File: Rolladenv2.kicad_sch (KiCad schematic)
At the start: 1 part, among them U1 ESP32-S3

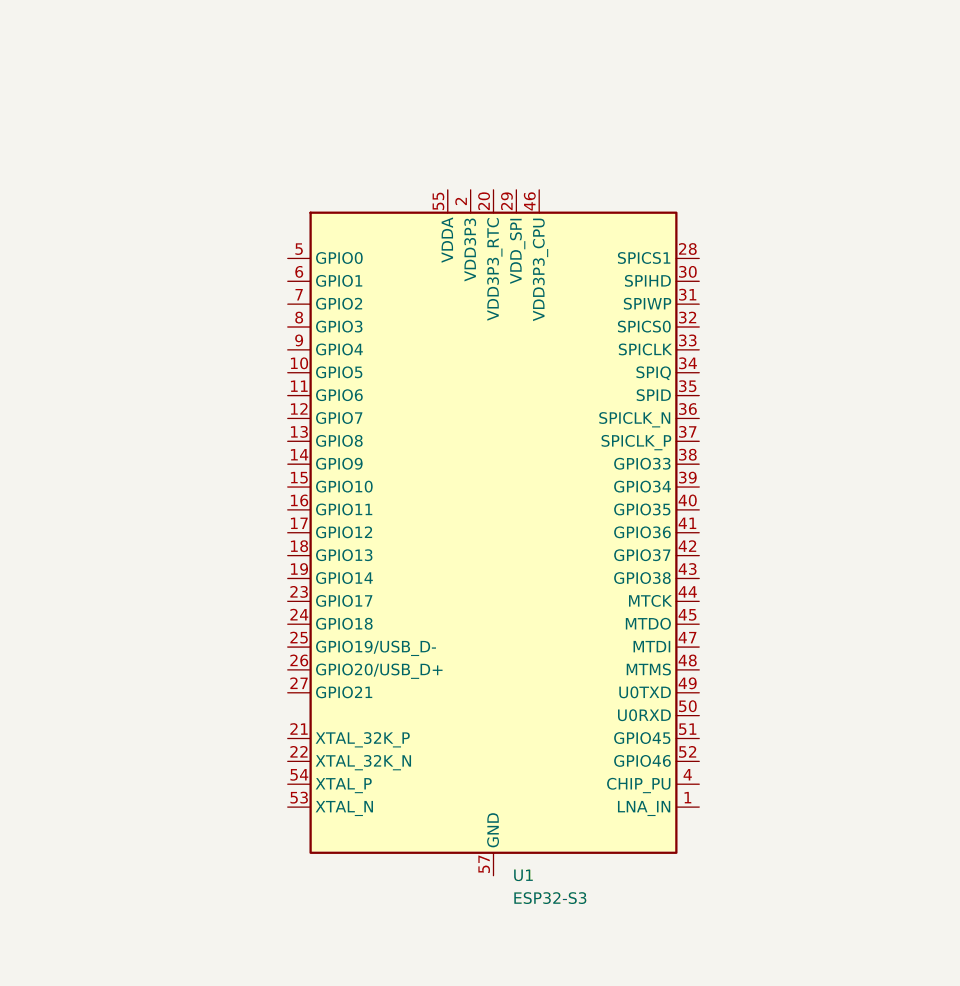
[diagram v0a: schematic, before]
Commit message: Added Caps and XTAL
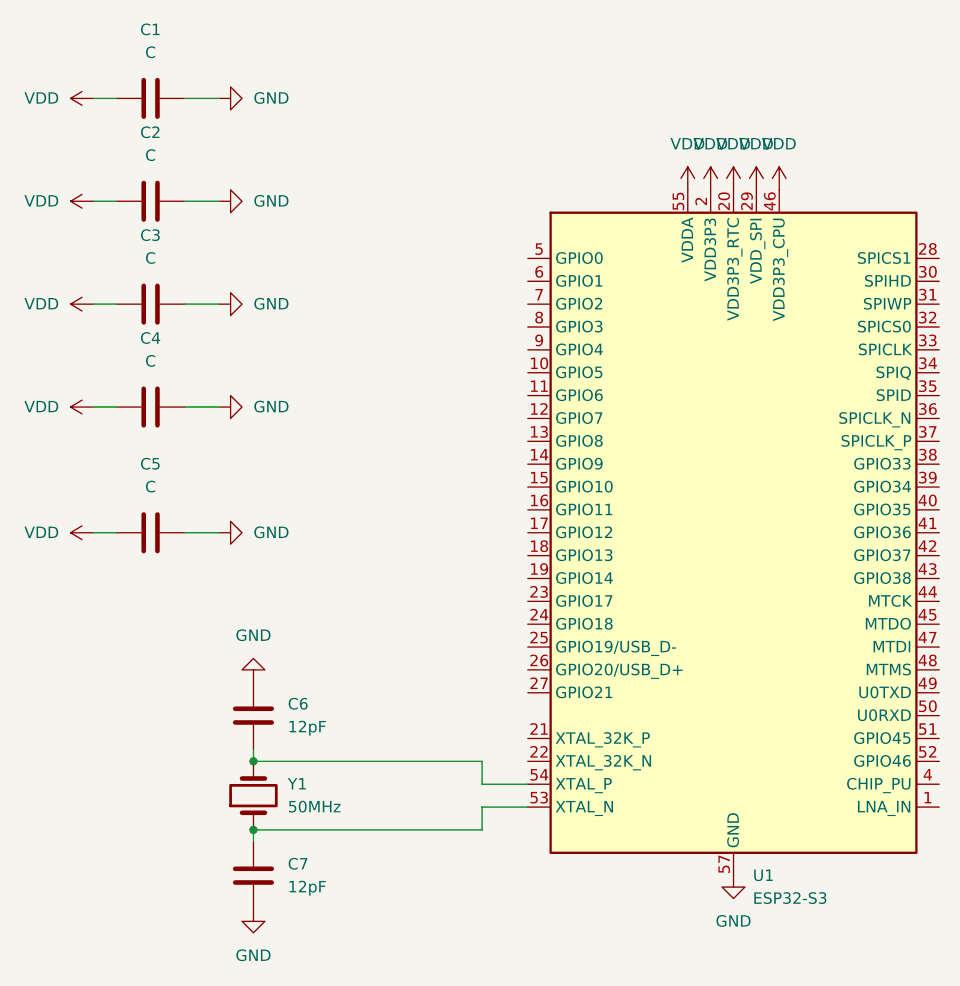
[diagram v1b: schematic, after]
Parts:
- added C1, C2, C3, C4, C5: C, Capacitor_SMD:C_0805_2012Metric_Pad1.18x1.45mm_HandSolder, symbol Device:C
- added C6, C7: 12pF, Capacitor_SMD:C_0603_1608Metric_Pad1.08x0.95mm_HandSolder, symbol Device:C
- added Y1: 50MHz, Crystal:Crystal_SMD_MicroCrystal_CC4V-T1A-2Pin_5.0x1.9mm_HandSoldering, symbol Device:Crystal
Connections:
- net VDD: now reaches U1.2 (VDD3P3), U1.3 (VDD3P3)
- net VDD: now also U1.20 (VDD3P3_RTC), U1.29 (VDD_SPI), U1.46 (VDD3P3_CPU), U1.55 (VDDA), U1.56 (VDDA), C1.1, C2.1, C3.1, C4.1, C5.1
- net at U1.53 (XTAL_N): now also C7.2, Y1.1
- net at U1.54 (XTAL_P): now also C6.2, Y1.2
- net GND: now reaches U1.57 (GND)
- net GND: now also C1.2, C2.2, C3.2, C4.2, C5.2, C6.1, C7.1
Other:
- moved on the sheet: U1

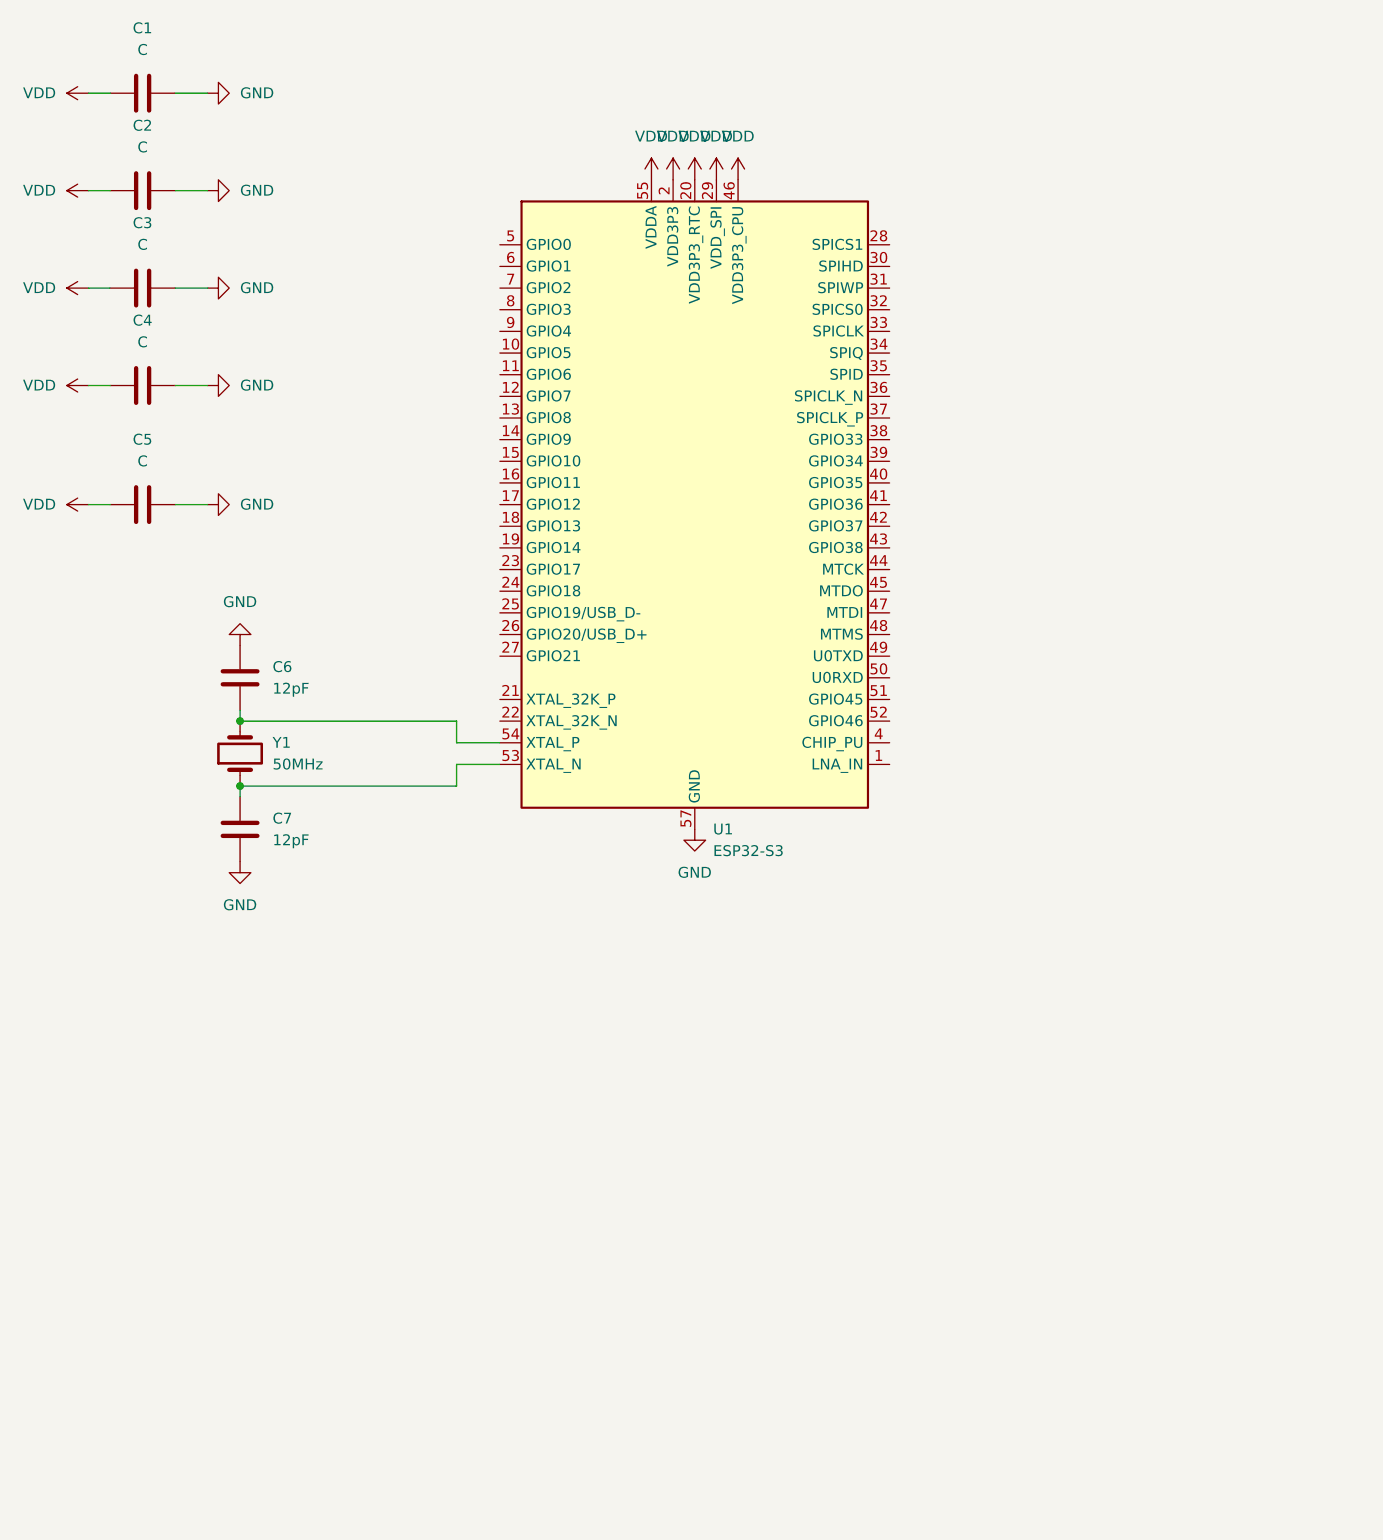
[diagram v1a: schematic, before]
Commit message: Added Reset Circuitry
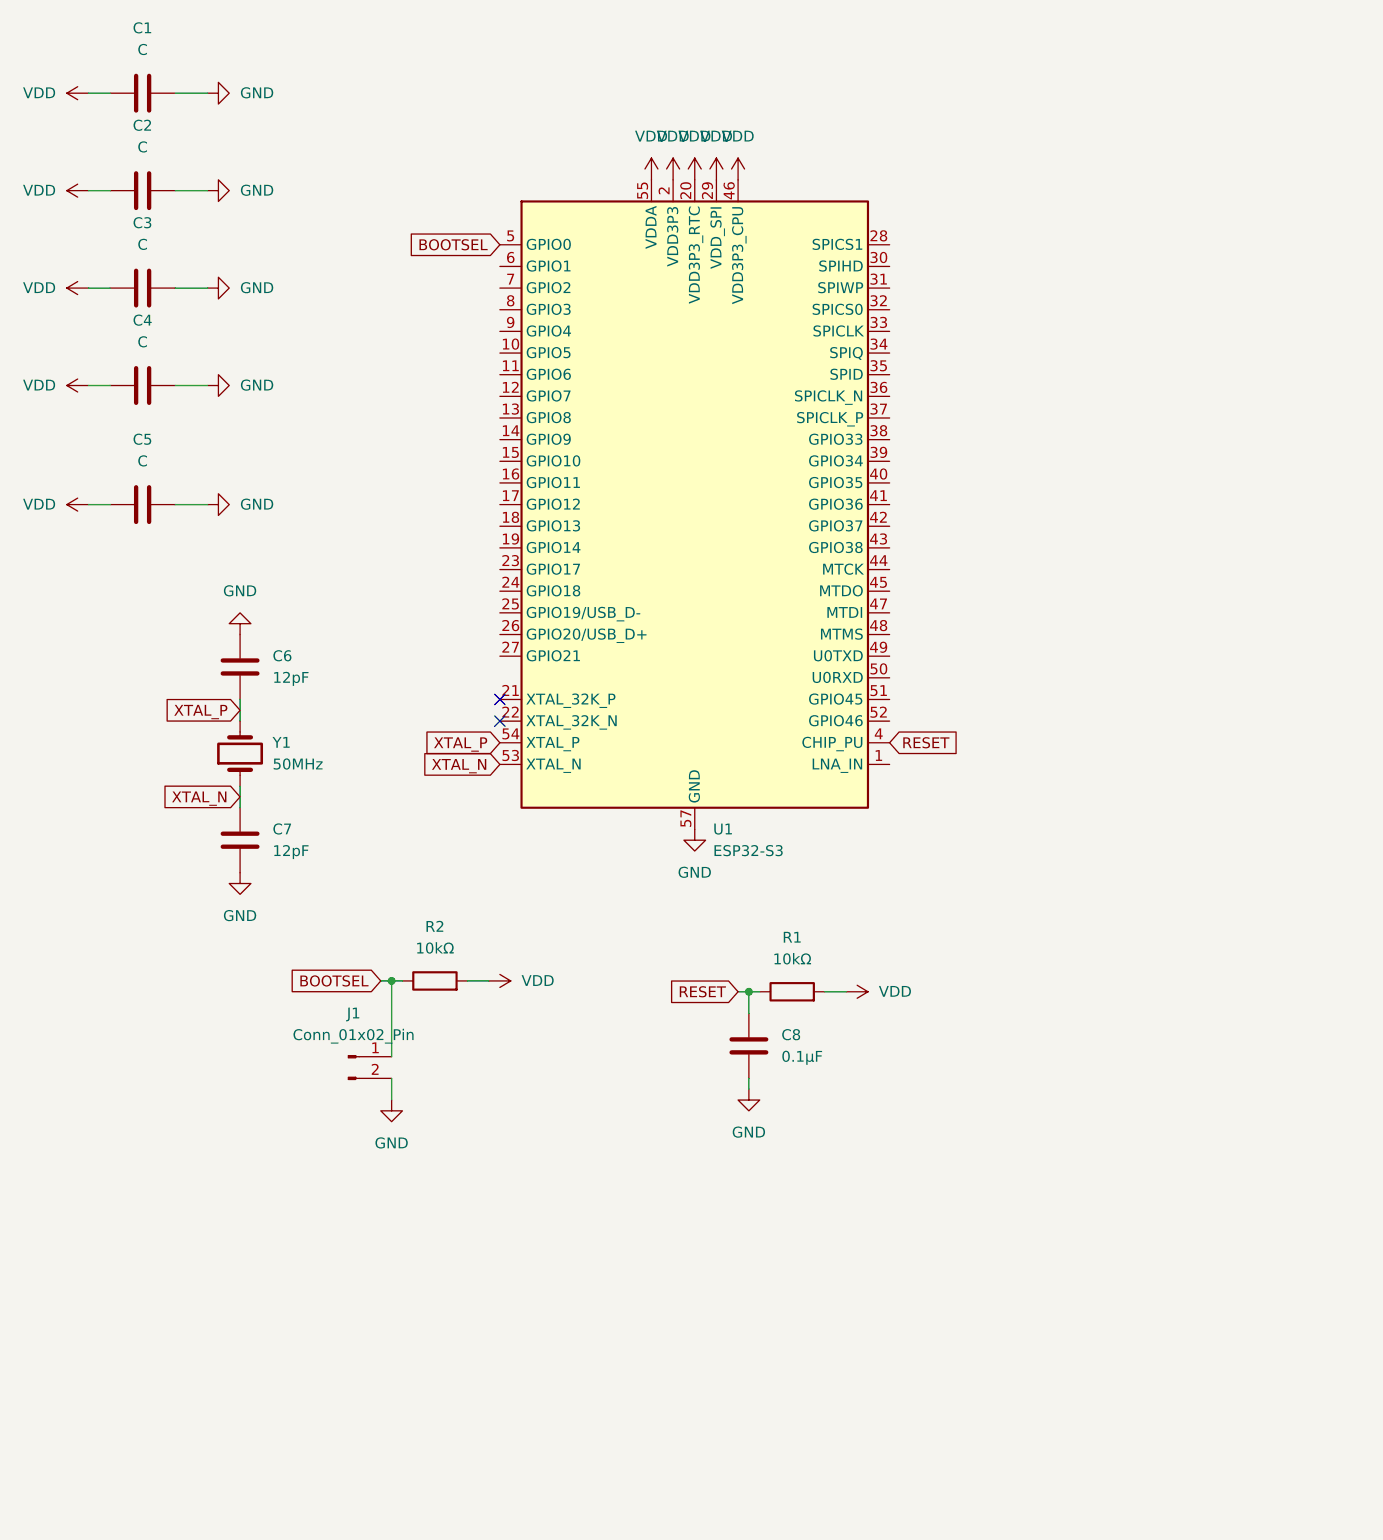
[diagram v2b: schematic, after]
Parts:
- added C8: 0.1µF, Capacitor_SMD:C_0805_2012Metric_Pad1.18x1.45mm_HandSolder, symbol Device:C
- added J1: Conn_01x02_Pin, Connector_PinHeader_2.54mm:PinHeader_1x02_P2.54mm_Vertical, symbol Connector:Conn_01x02_Pin
- added R1, R2: 10kΩ, Resistor_SMD:R_0805_2012Metric_Pad1.20x1.40mm_HandSolder, symbol Device:R
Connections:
- net GND: now also C8.2, J1.2 (Pin_2)
- net VDD: now also R1.2, R2.2
- net XTAL_P: now reaches C6.2, U1.54 (XTAL_P), Y1.2
- net RESET: now reaches U1.4 (CHIP_PU)
- net RESET: now also C8.1, R1.1
- net BOOTSEL: now reaches U1.5 (GPIO0)
- net BOOTSEL: now also J1.1 (Pin_1), R2.1
- net XTAL_N: now reaches C7.2, U1.53 (XTAL_N), Y1.1
- no-connect marks 0 -> 2
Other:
- moved on the sheet: C6, C7

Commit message: Added Flash Data
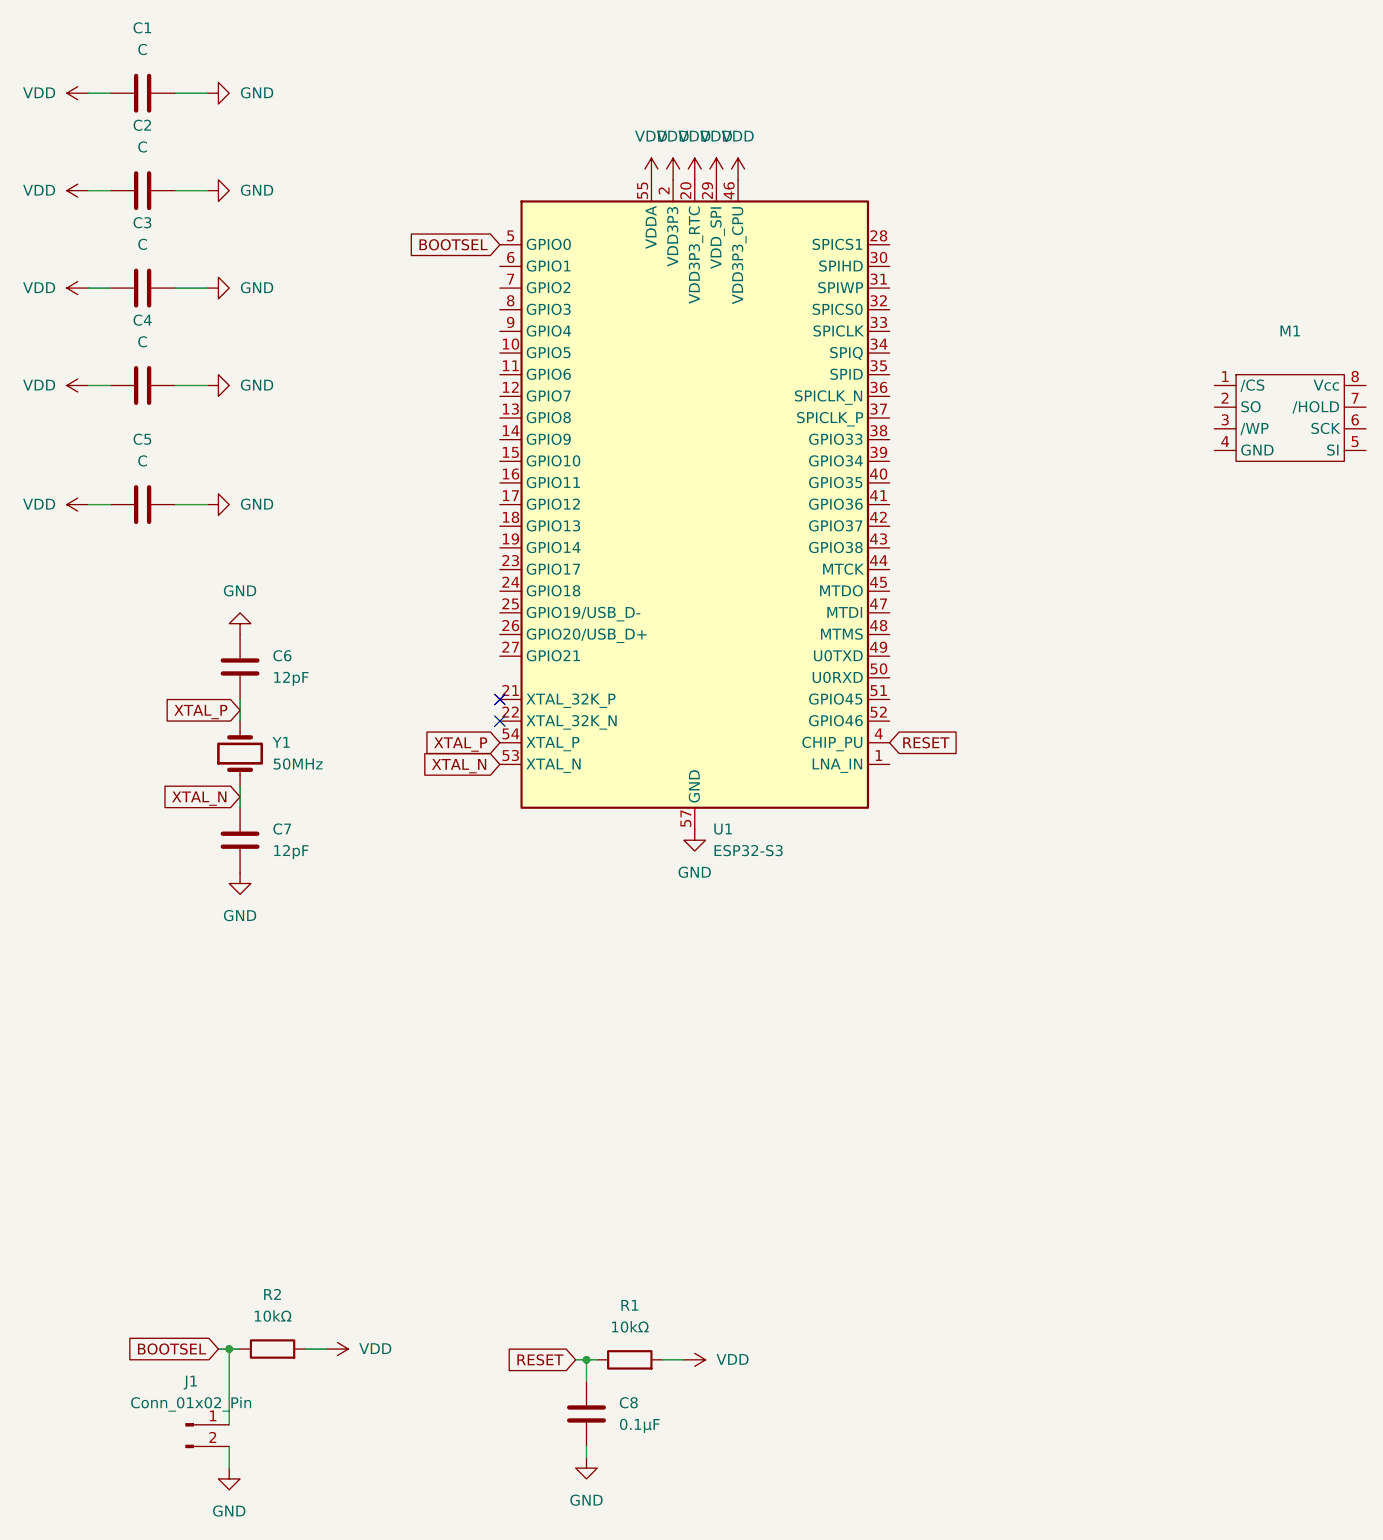
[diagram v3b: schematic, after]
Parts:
- added M1: ~, AT25SL641-MHE-T:SON127P500X600X60-9N, symbol Symbols:AT25SL641-MHE-T
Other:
- moved on the sheet: C8, J1, R1, R2
